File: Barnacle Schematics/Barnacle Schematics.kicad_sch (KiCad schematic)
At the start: 17 parts, among them M3 MG996, M4 SG90, SW1 Reset, U1 TiVa

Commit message: power global bariable and some other update
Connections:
- net Dump_Servo/ OC3: now also UA1.10 (RA3); no longer UA1.9 (RA2)
- net Connection Indicator/ OC4: now reaches M4.1 (PWM)
- net Connection Indicator/ OC4: now also UA1.9 (RA2)
- no-connect marks 29 -> 28
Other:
- moved on the sheet: C1, C2, C3, C4, ESC1, ESC2, M1, M2, PRG1, R1, R2, SW1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

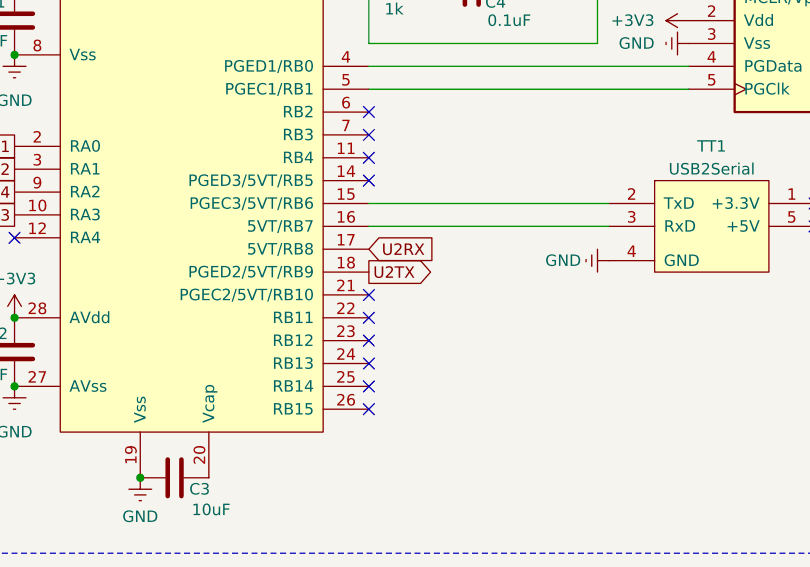
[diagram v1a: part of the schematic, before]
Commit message: charging function fix
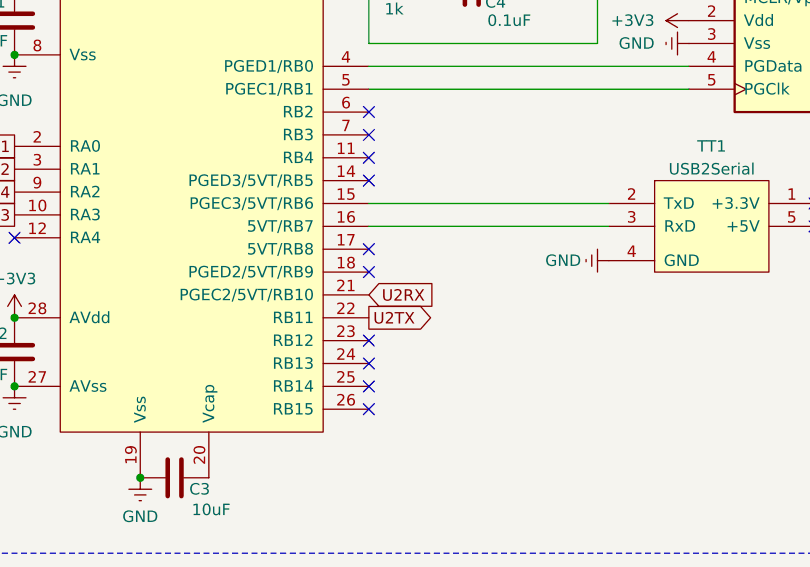
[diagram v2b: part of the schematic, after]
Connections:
- net U2RX: now also UA1.21 (PGEC2/5VT/RB10); no longer UA1.17 (5VT/RB8)
- net U2TX: now also UA1.22 (RB11); no longer UA1.18 (PGED2/5VT/RB9)
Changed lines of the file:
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@@
-	)
-	(no_connect
-		(at 83.82 67.31)
 	)
 	(no_connect
@@
 	)
 	(no_connect
-		(at 83.82 64.77)
-	)
-	(no_connect
 		(at 83.82 72.39)
 	)
@@
 	(no_connect
 		(at 66.04 130.81)
+	)
+	(no_connect
+		(at 83.82 59.69)
+	)
+	(no_connect
+		(at 83.82 62.23)
 	)
 	(no_connect
@@
 		)
 	)
-	(global_label "U2TX"
-		(shape output)
-		(at 83.82 62.23 0)
-		(fields_autoplaced yes)
-		(effects
-			(font
-				(size 1.27 1.27)
-			)
-			(justify left)
-		)
-		(property "Intersheetrefs" "${INTERSHEET_REFS}"
-			(at 91.5223 62.23 0)
-			(effects
-				(font
-					(size 1.27 1.27)
-				)
-				(justify left)
-				(hide yes)
-			)
-		)
-	)
 	(global_label "Left_PWM{slash} OC1"
 		(shape output)
@@
 		)
 	)
-	(global_label "U2RX"
-		(shape input)
-		(at 83.82 59.69 0)
+	(global_label "U2TX"
+		(shape output)
+		(at 83.82 67.31 0)
 		(fields_autoplaced yes)
 		(effects
@@
 		)
 		(property "Intersheetrefs" "${INTERSHEET_REFS}"
-			(at 91.8247 59.69 0)
+			(at 91.5223 67.31 0)
 			(effects
 				(font
@@
 				(hide yes)
 			)
+		)
+	)
+	(global_label "U2RX"
+		(shape input)
+		(at 83.82 64.77 0)
+		(fields_autoplaced yes)
+		(effects
+			(font
+				(size 1.27 1.27)
+			)
+			(justify left)
+		)
+		(property "Intersheetrefs" "${INTERSHEET_REFS}"
+			(at 91.8247 64.77 0)
+			(effects
+				(font
+					(size 1.27 1.27)
+				)
+				(justify left)
+				(hide yes)
+			)

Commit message: try merge with main after final
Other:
- note added: "Servo"
- note added: "Thrusters"
- note added: "XBee Connection"
- note removed: "Thruster"
- company: (none) -> Team 6
- title: (none) -> BARNACLE Schematics
- moved on the sheet: ESC1, ESC2, M1, M2, M3, M4, U1A
